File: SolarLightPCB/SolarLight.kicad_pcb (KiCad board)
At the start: 2 copper layers, 99.5 x 45 mm, 19 parts, among them J1 I2C, J2 SPI, J3 SCK Jumper, J4 ADC, U1 TP4056, U2 WeMos_D1_mini, U3 L78L33_TO92

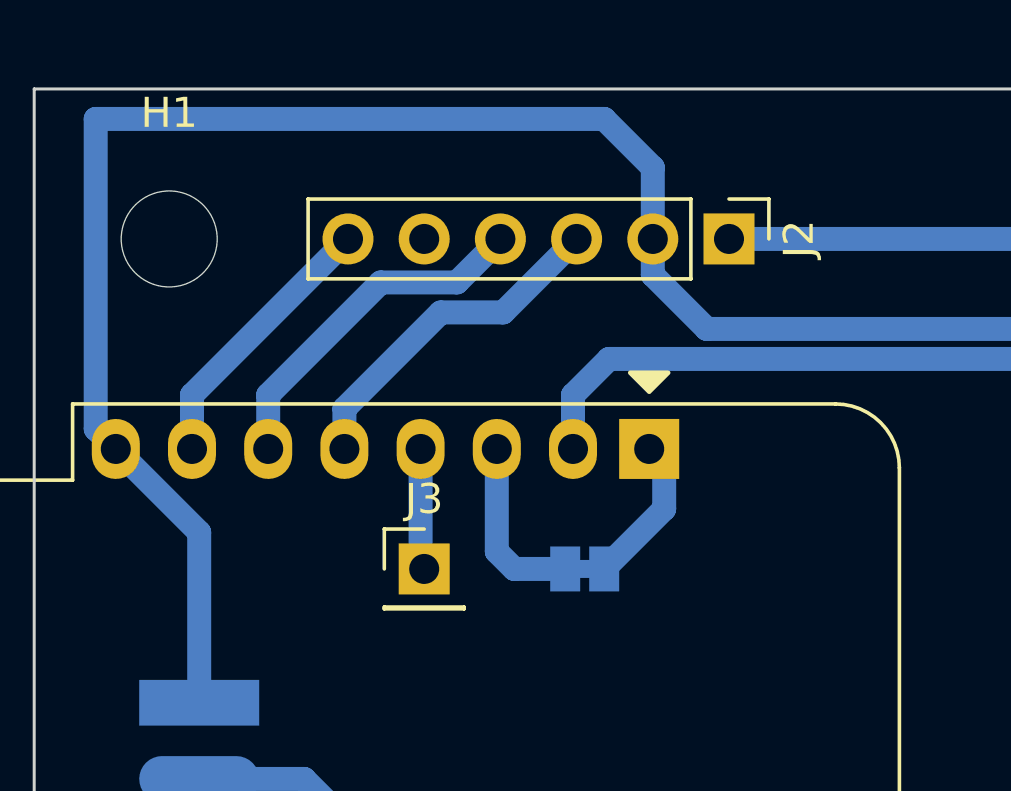
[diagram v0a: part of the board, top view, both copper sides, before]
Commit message: Replace the missing connection with a jumper
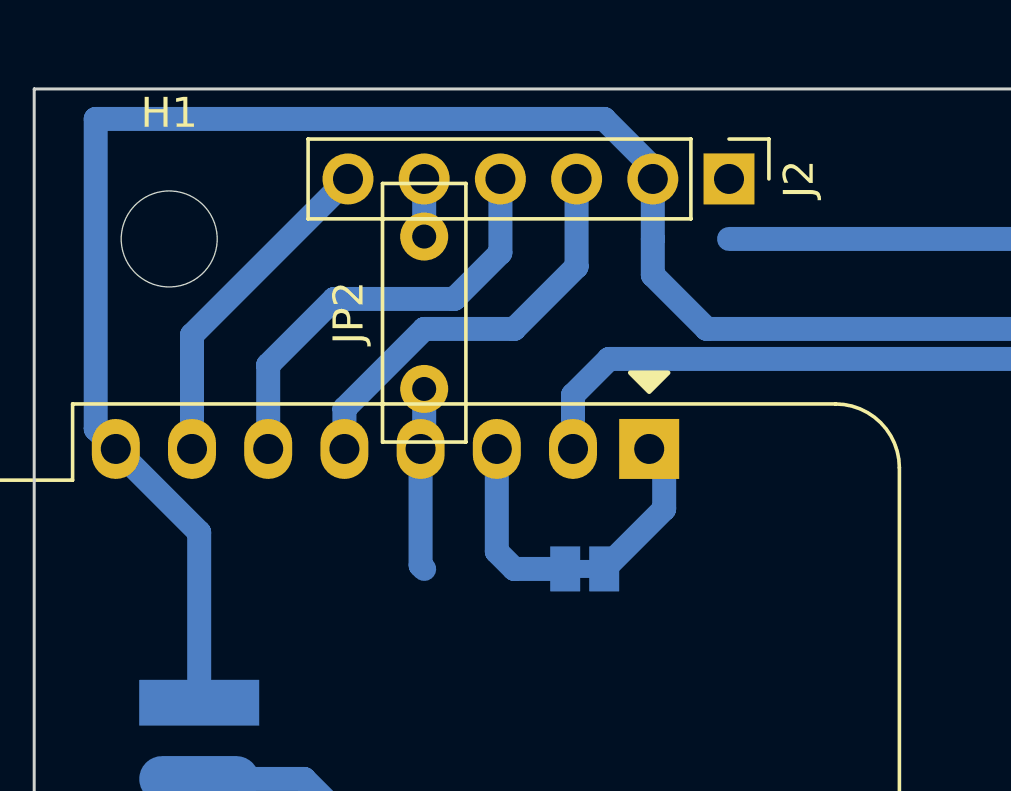
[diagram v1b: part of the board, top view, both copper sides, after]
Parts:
- removed J3: SCK Jumper, Connector_PinHeader_2.54mm:PinHeader_1x01_P2.54mm_Vertical
- added JP2: Bridge, Resistor_THT:R_Box_L8.4mm_W2.5mm_P5.08mm, F.Cu at (93.0, 65.0)
- moved J2 2.00 mm to (103.2, 58.0)
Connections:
- J2 pad 5: SCK -> Net-(J2-Pad5)
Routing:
- net MOSI: track 11.7 -> 14.5 mm
- net MISO: track 11.4 -> 14.0 mm
- net SCK: track 4.22 -> 6.27 mm
- net CS: track 9.15 -> 11.2 mm
- net Net-(J2-Pad5): track 0.00 -> 1.92 mm

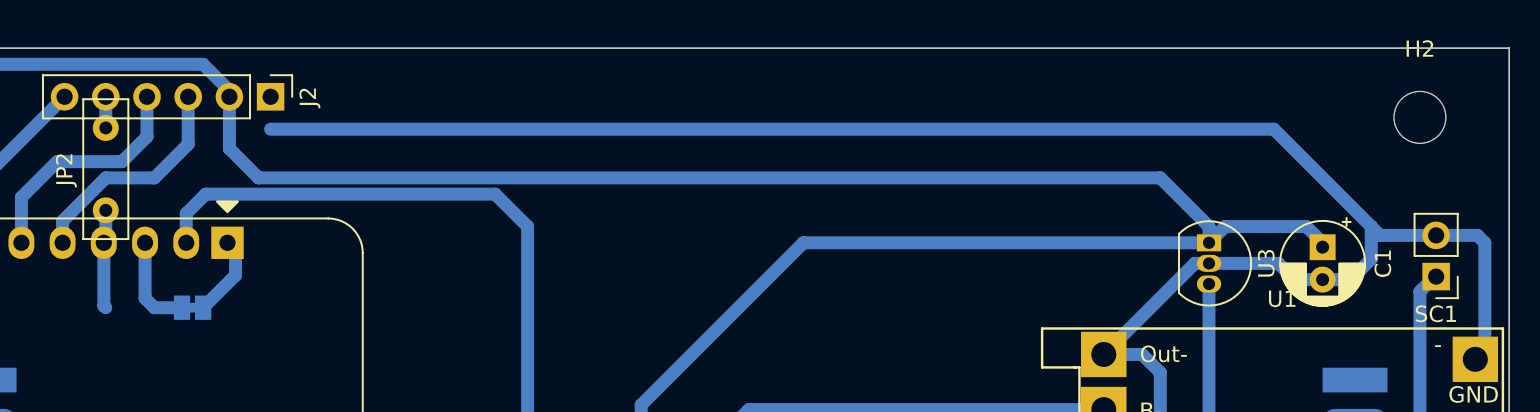
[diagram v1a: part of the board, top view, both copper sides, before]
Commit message: Add missing trace
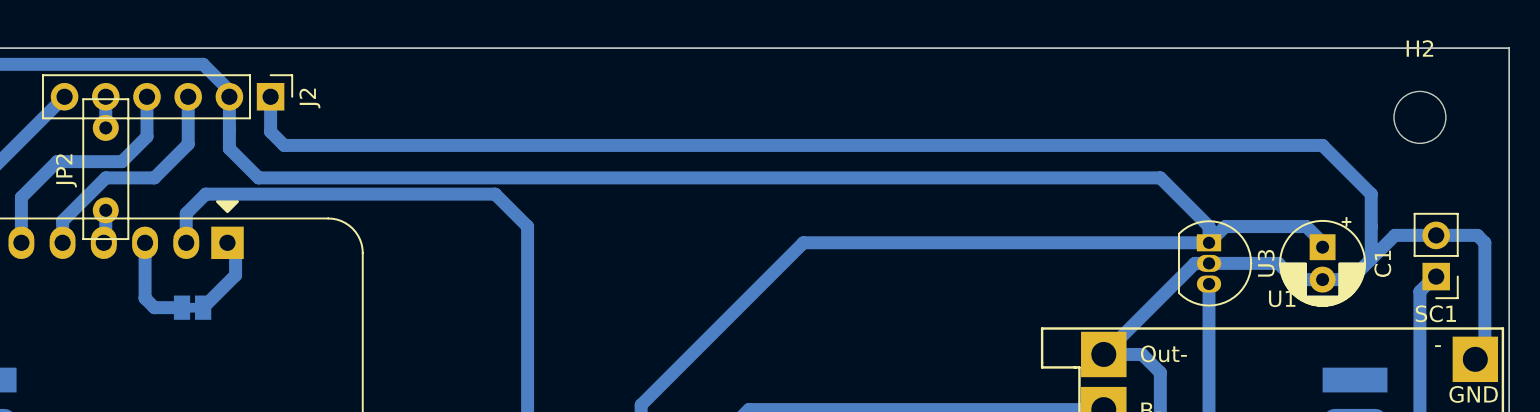
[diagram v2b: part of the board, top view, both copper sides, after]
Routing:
- net SCK: track 6.27 -> 2.22 mm
- net GND: track 212.2 -> 215.9 mm
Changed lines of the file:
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@@
   (segment (start 106.599261 99.139261) (end 117.860739 99.139261) (width 0.8) (layer "B.Cu") (net 4))
   (segment (start 104.46 97) (end 102.46 99) (width 0.8) (layer "B.Cu") (net 4))
-  (segment (start 171.5425 66.5425) (end 175 66.5425) (width 0.8) (layer "B.Cu") (net 4))
   (segment (start 156.8825 73.8825) (end 154.5125 73.8825) (width 0.8) (layer "B.Cu") (net 4))
+  (segment (start 172.4575 66.5425) (end 175 66.5425) (width 0.8) (layer "B.Cu") (net 4))
   (segment (start 171 66) (end 171 68) (width 0.8) (layer "B.Cu") (net 4))
   (segment (start 102.46 99) (end 92.46 99) (width 0.8) (layer "B.Cu") (net 4))
+  (segment (start 103.16 60.16) (end 104 61) (width 0.8) (layer "B.Cu") (net 4))
   (segment (start 158 75) (end 156.8825 73.8825) (width 0.8) (layer "B.Cu") (net 4))
   (segment (start 158 79) (end 158 75) (width 0.8) (layer "B.Cu") (net 4))
@@
   (segment (start 92.46 99) (end 90.46 97) (width 0.8) (layer "B.Cu") (net 4))
   (segment (start 161 68.27) (end 160.125 68.27) (width 0.8) (layer "B.Cu") (net 4))
-  (segment (start 165 60) (end 171 66) (width 0.8) (layer "B.Cu") (net 4))
   (segment (start 85.26 81.26) (end 85.26 89.86) (width 0.8) (layer "B.Cu") (net 4))
   (segment (start 85.26 89.86) (end 85.26 90.26) (width 0.8) (layer "B.Cu") (net 4))
+  (segment (start 171 64) (end 171 66) (width 0.8) (layer "B.Cu") (net 4))
+  (segment (start 168 61) (end 171 64) (width 0.8) (layer "B.Cu") (net 4))
   (segment (start 157 80) (end 158 79) (width 0.8) (layer "B.Cu") (net 4))
-  (segment (start 103.16 60) (end 165 60) (width 0.8) (layer "B.Cu") (net 4))
+  (segment (start 104 61) (end 168 61) (width 0.8) (layer "B.Cu") (net 4))
   (segment (start 104.46 97) (end 106.599261 99.139261) (width 0.8) (layer "B.Cu") (net 4))
   (segment (start 129 88) (end 138 88) (width 0.8) (layer "B.Cu") (net 4))
+  (segment (start 171 68) (end 172.4575 66.5425) (width 0.8) (layer "B.Cu") (net 4))
   (segment (start 166.27 69.27) (end 168 69.27) (width 0.8) (layer "B.Cu") (net 4))
   (segment (start 165.27 68.27) (end 166.27 69.27) (width 0.8) (layer "B.Cu") (net 4))
-  (segment (start 171 66) (end 171.5425 66.5425) (width 0.8) (layer "B.Cu") (net 4))
   (segment (start 178 67) (end 178 73.595) (width 0.8) (layer "B.Cu") (net 4))
   (segment (start 161 68.27) (end 165.27 68.27) (width 0.8) (layer "B.Cu") (net 4))
   (segment (start 85 81) (end 85.26 81.26) (width 0.25) (layer "B.Cu") (net 4))
+  (segment (start 103.16 58) (end 103.16 60.16) (width 0.8) (layer "B.Cu") (net 4))
   (segment (start 85.26 90.26) (end 90.46 95.46) (width 0.8) (layer "B.Cu") (net 4))
   (segment (start 160.125 68.27) (end 154.5125 73.8825) (width 0.8) (layer "B.Cu") (net 4))
@@
   (segment (start 95.42 67) (end 95.42 70.42) (width 0.8) (layer "B.Cu") (net 11))
   (segment (start 96 71) (end 97.7 71) (width 0.8) (layer "B.Cu") (net 11))
-  (segment (start 92.88 67) (end 92.88 70.88) (width 0.8) (layer "B.Cu") (net 12))
   (segment (start 93 67.12) (end 92.88 67) (width 0.8) (layer "B.Cu") (net 12))
   (segment (start 93 66.88) (end 92.88 67) (width 0.8) (layer "B.Cu") (net 12))
   (segment (start 93 65) (end 93 66.88) (width 0.8) (layer "B.Cu") (net 12))
-  (segment (start 92.88 70.88) (end 93 71) (width 0.8) (layer "B.Cu") (net 12))
   (segment (start 90.34 67) (end 90.34 65.66) (width 0.8) (layer "B.Cu") (net 13))
   (segment (start 98.08 60.92) (end 98.08 58) (width 0.8) (layer "B.Cu") (net 13))

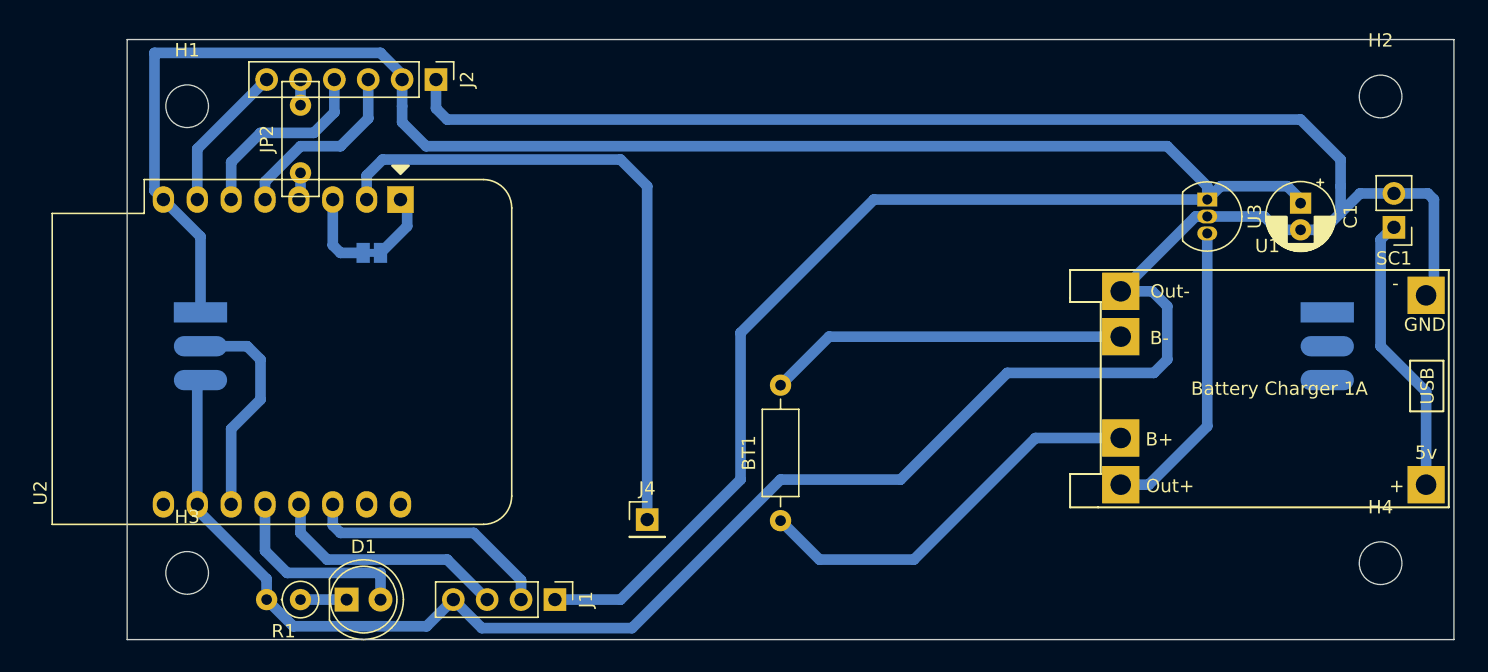
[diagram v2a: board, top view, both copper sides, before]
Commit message: Add voltage divider to measure the battery voltage
fixes #4
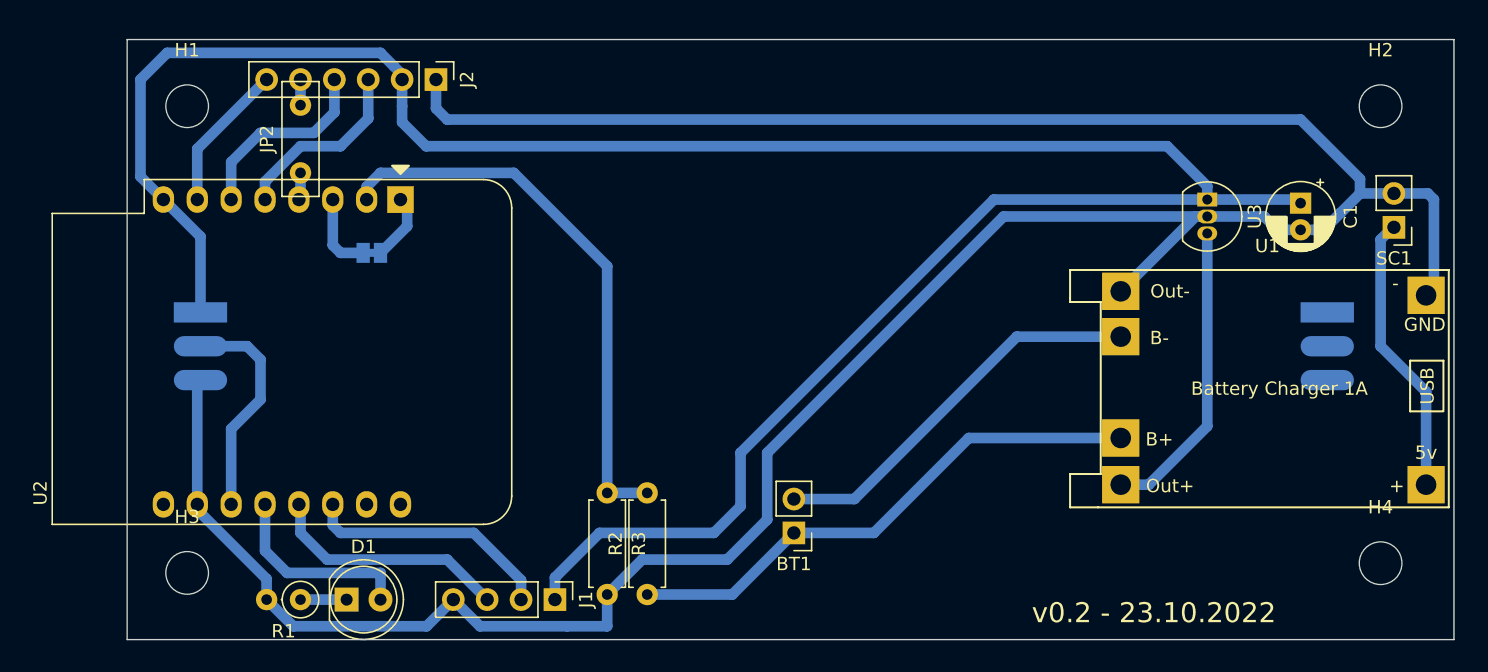
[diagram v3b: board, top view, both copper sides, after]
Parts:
- removed J4: ADC, Connector_PinHeader_2.54mm:PinHeader_1x01_P2.54mm_Vertical
- added R2: R, Resistor_THT:R_Axial_DIN0207_L6.3mm_D2.5mm_P7.62mm_Horizontal, F.Cu at (119.0, 96.6)
- added R3: R, Resistor_THT:R_Axial_DIN0207_L6.3mm_D2.5mm_P7.62mm_Horizontal, F.Cu at (116.0, 89.0)
- BT1: footprint Resistor_THT:R_Axial_DIN0207_L6.3mm_D2.5mm_P10.16mm_Horizontal -> Connector_PinHeader_2.54mm:PinHeader_1x02_P2.54mm_Vertical
- U3: value L78L33_TO92 -> MCP1700-3302E
- moved BT1 1.36 mm to (130.0, 92.0), turned to 180 degrees
- moved H2 0.73 mm to (174.0, 60.0)
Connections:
- U2 pad 2: ADC -> A0
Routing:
- net ADC: track 49.2 -> 0.00 mm
- net A0: track 0.00 -> 42.3 mm
- net BATTERY: track 30.5 -> 40.4 mm
- net +3V3: track 183.0 -> 179.5 mm
- net GND: track 215.9 -> 218.7 mm
- net Net-(BT1-Pad2): track 27.1 -> 29.6 mm
- net RST: track 5.04 -> 5.74 mm
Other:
- board text added: "v0.2 - 23.10.2022"

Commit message: Add a power on Jumper
fixes #5
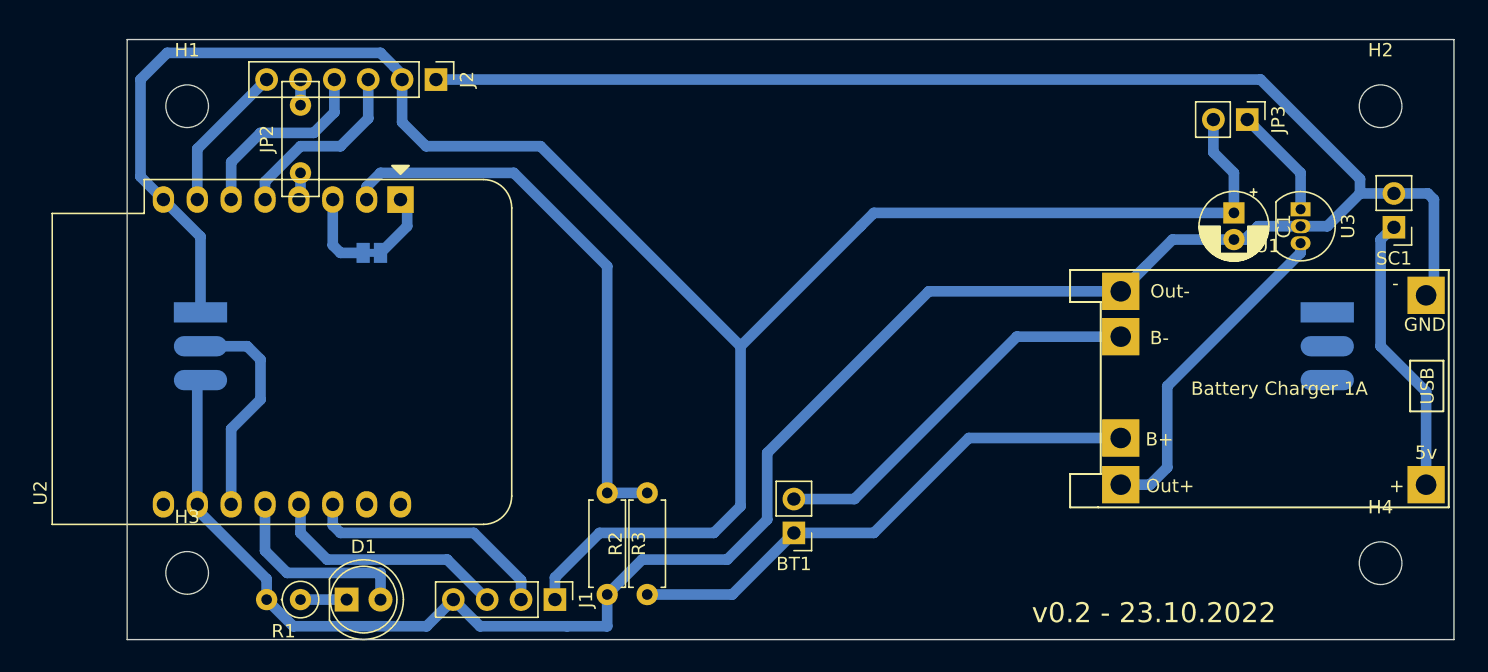
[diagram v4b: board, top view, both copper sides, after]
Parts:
- added JP3: POWER ON, Connector_PinHeader_2.54mm:PinHeader_1x02_P2.54mm_Vertical, F.Cu at (164.0, 61.0)
- moved U3 7.04 mm to (168.0, 67.7)
- moved C1 5.05 mm to (163.0, 68.0)
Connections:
- U3 pad 1: +3V3 -> Net-(U3-Pad1)
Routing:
- net +3V3: track 179.5 -> 155.3 mm
- net Net-(U3-Pad1): track 0.00 -> 8.39 mm
- net GND: track 218.7 -> 210.5 mm
- net Net-(U1-Pad3): track 22.8 -> 25.0 mm

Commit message: Minor changes to PCB
- Added _draft_ mounting holes
- Added SPI and I2C labels
- Changed the Board dimension to 100x45mm
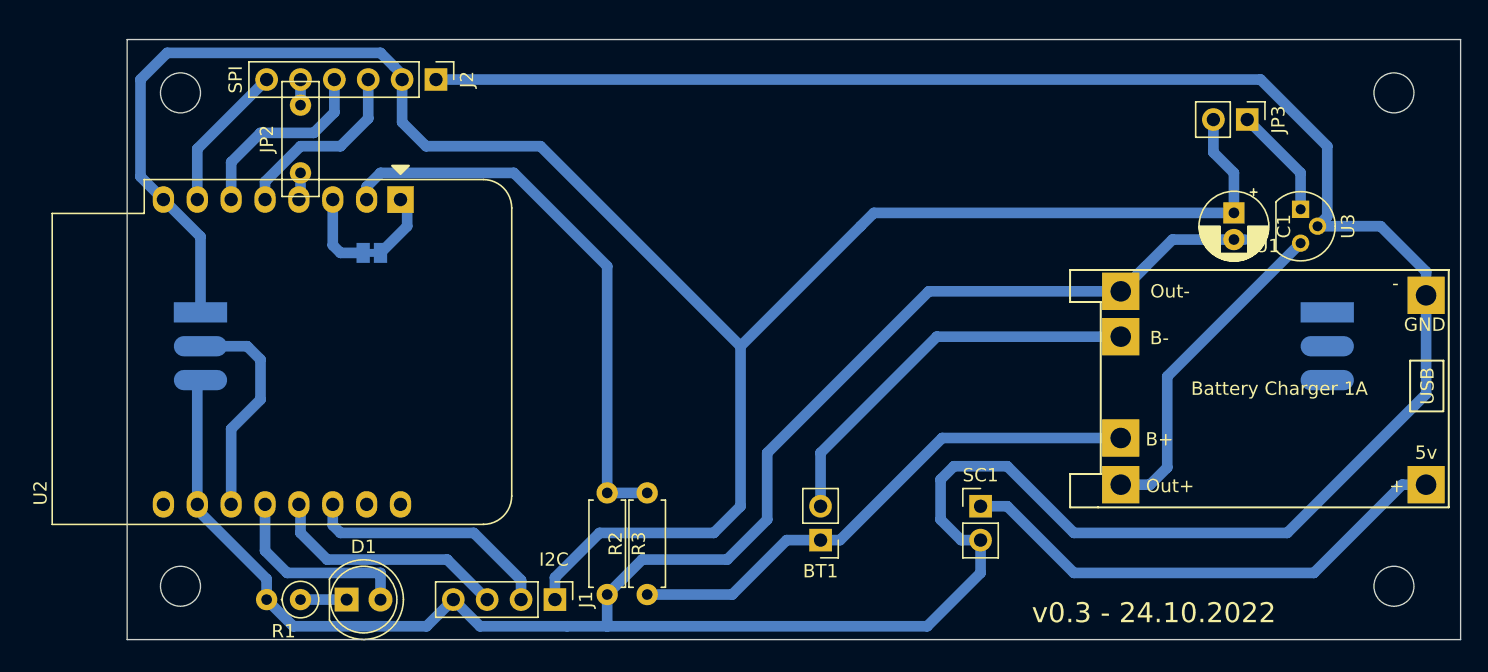
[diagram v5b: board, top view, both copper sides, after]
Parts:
- removed H1, H2, H3, H4: MountingHole, MountingHole:MountingHole_3.2mm_M3
- U3: footprint Package_TO_SOT_THT:TO-92_Inline -> Package_TO_SOT_THT:TO-92
- moved SC1 37.4 mm to (144.0, 90.0), turned to 0 degrees
- moved BT1 2.07 mm to (132.0, 92.5)
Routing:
- net GND: track 210.5 -> 290.5 mm
- net Net-(SC1-Pad1): track 21.2 -> 38.2 mm
- net Net-(BT1-Pad2): track 29.6 -> 30.1 mm
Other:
- board size 99.5 x 45 mm -> 100 x 45 mm
- board text added: "H4"
- board text added: "v0.3 - 24.10.2022"
- board text removed: "v0.2 - 23.10.2022"
